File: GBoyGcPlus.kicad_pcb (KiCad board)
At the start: 2 copper layers, 62.9 x 53.1 mm, 43 parts, among them J1 Conn_01x06, J2 Conn_01x06, J3 Left Stick, J4 Right Stick, SW1 RKA2SGG055SMTR LFS, SW2 RKA2SGG055SMTR LFS, SW3 RKA2SGG055SMTR LFS, SW4 RKA2SGG055SMTR LFS, SW5 RKA2SGG055SMTR LFS, SW6 RKA2SGG055SMTR LFS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

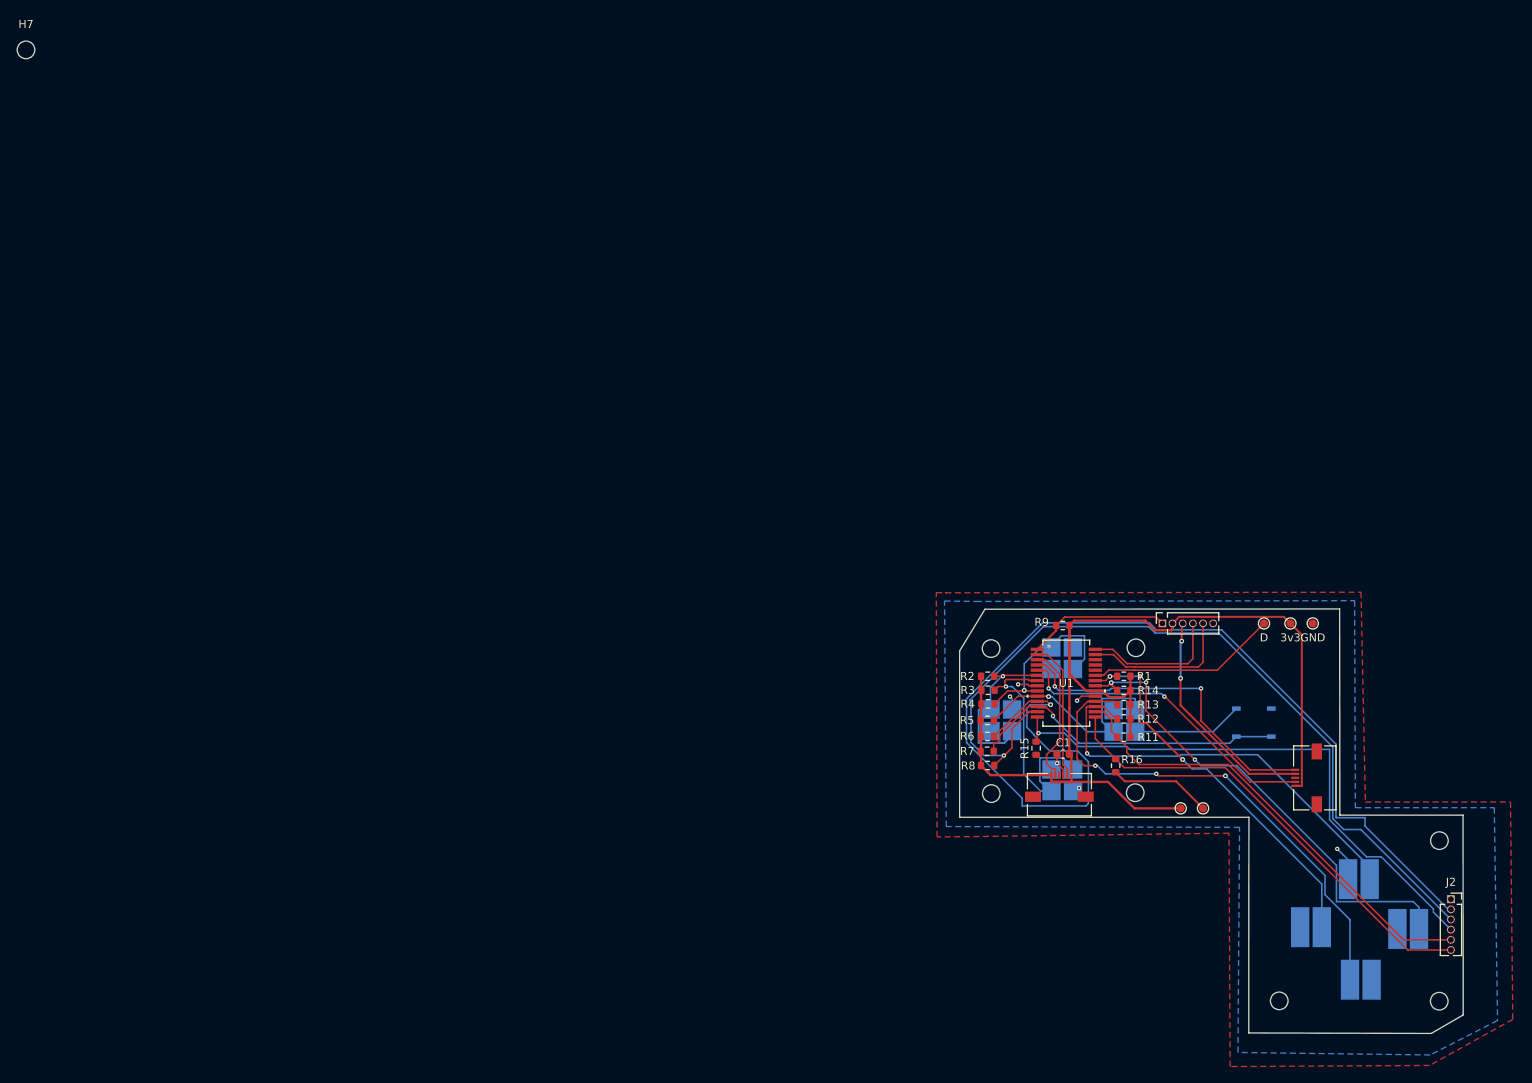
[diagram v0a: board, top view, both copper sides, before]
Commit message: Changed PCB to use GC2 Micro controller
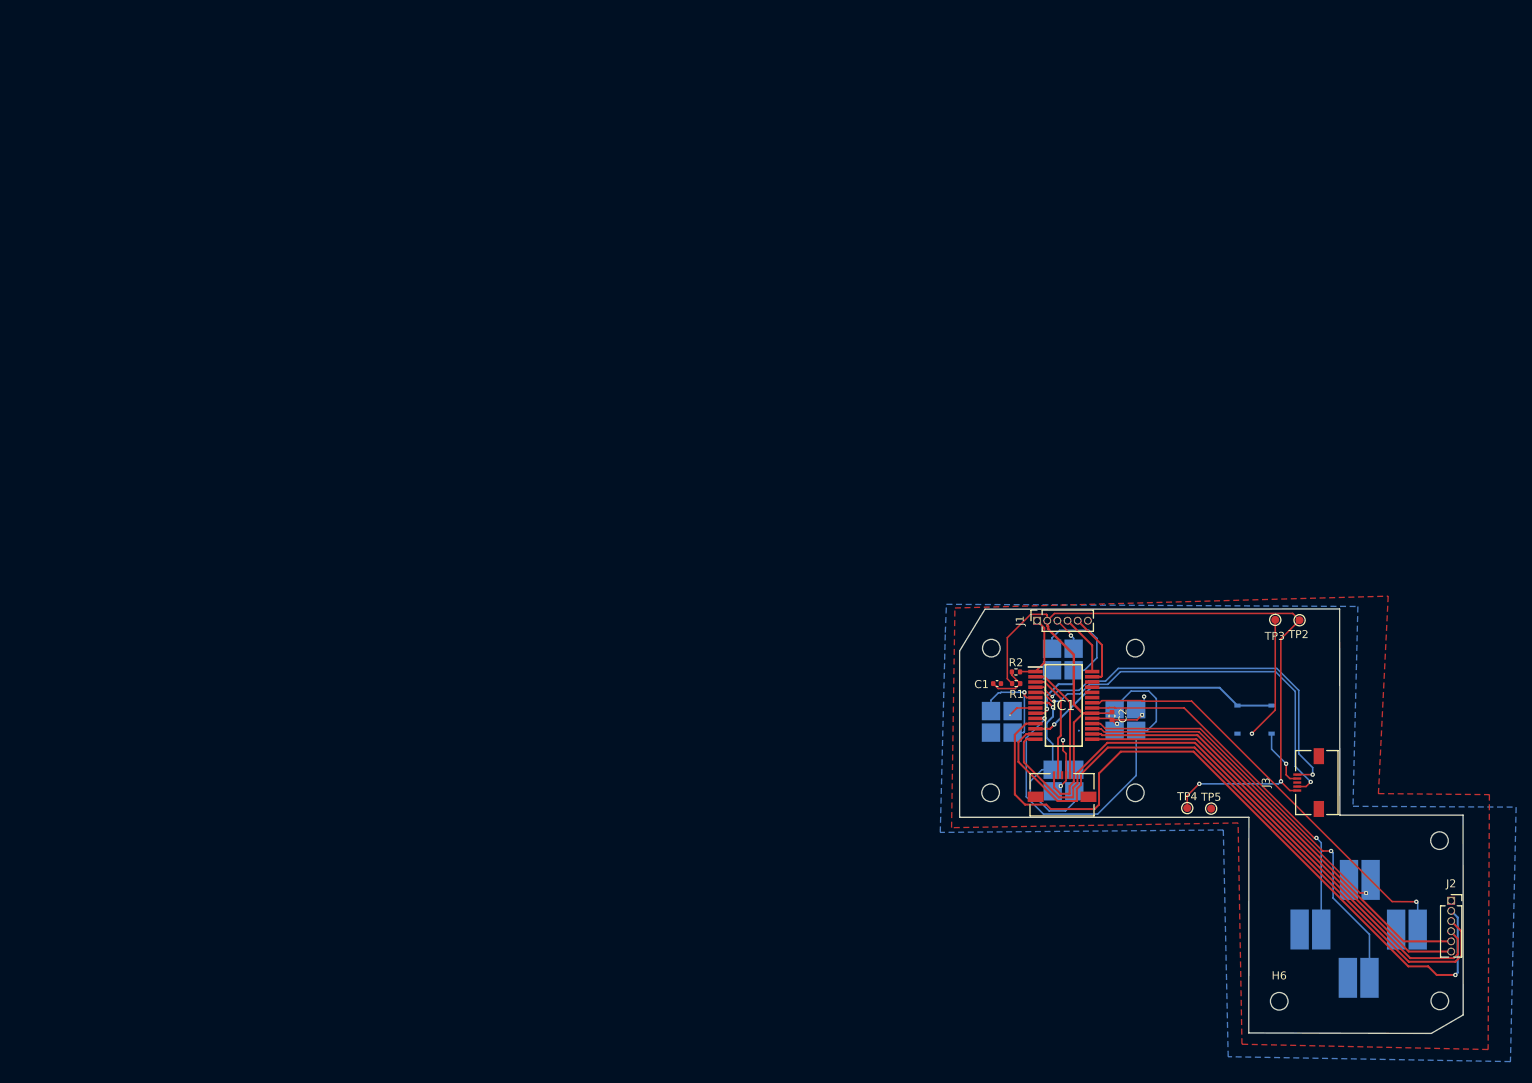
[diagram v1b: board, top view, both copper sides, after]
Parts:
- removed 3v3: 3v3, TestPoint:TestPoint_Pad_D1.0mm
- removed D: D, TestPoint:TestPoint_Pad_D1.0mm
- removed GND: Gnd, TestPoint:TestPoint_Pad_D1.0mm
- removed H4: MountingHole, MountingHole:MountingHole_2.2mm_M2
- removed R11, R12, R13, R14, R15, R16, R3, R4, R5, R6, R7, R8, R9: 10k, Resistor_SMD:R_0603_1608Metric
- removed U1: pic18f25k22-i/ss, GCPlus:SSOP28_MC_MCH
- added C2: 0.1uf, Capacitor_SMD:C_0402_1005Metric, F.Cu at (138.2, 85.7)
- added IC1: PIC18F25K42-I_SS, GCPlus:SOP65P780X200-28N, F.Cu at (132.2, 84.4)
- added TP2: 3v3, TestPoint:TestPoint_Pad_D1.0mm, F.Cu at (161.7, 73.8)
- added TP3: Gnd, TestPoint:TestPoint_Pad_D1.0mm, F.Cu at (158.6, 73.7)
- C1: value 100 nF -> 0.1uF; footprint Capacitor_SMD:C_0603_1608Metric -> Capacitor_SMD:C_0402_1005Metric
- R1: footprint Resistor_SMD:R_0603_1608Metric -> Resistor_SMD:R_0402_1005Metric
- R2: value 10k -> 1000Ohm; footprint Resistor_SMD:R_0603_1608Metric -> Resistor_SMD:R_0402_1005Metric
- SW5, SW6, SW7, SW8: footprint footprints:DPAD -> GCPlus:DPAD
- SW9: footprint footprints:RKA2SG_CNK -> GCPlus:RKA2SG_CNK-L
- moved H7 202.5 mm to (179.2, 101.3)
- moved H3 25.6 mm to (141.1, 77.3)
- moved H1 25.5 mm to (141.1, 95.3)
- moved H5 18.1 mm to (123.1, 77.3)
- moved H2 18.1 mm to (123.0, 95.3)
- moved J1 15.7 mm to (128.9, 73.8)
- moved R1 13.5 mm to (126.2, 81.7)
- moved SW6 12.2 mm to (164.4, 112.4)
- moved C1 12.1 mm to (123.9, 81.7)
- moved SW5 12.0 mm to (176.4, 112.4)
- moved R2 3.58 mm to (126.2, 80.2)
- moved SW3 2.79 mm to (133.4, 77.3), turned to 180 degrees
- moved SW1 2.51 mm to (125.8, 85.1), turned to 180 degrees
- moved SW7 2.44 mm to (170.4, 118.5), turned to 180 degrees
- moved TP5 1.01 mm to (150.6, 97.3)
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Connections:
- C1 pad 1: GND -> Net-(C1-Pad1)
- C1 pad 2: +3V3 -> GND
- R1 pad 1: /DL -> +3V3
- R1 pad 2: +3V3 -> Net-(C1-Pad1)
- R2 pad 1: +3V3 -> Net-(C1-Pad1)
- R2 pad 2: /A -> /MCLR
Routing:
- net /Z: track 139.3 -> 91.7 mm
- net Net-(U1-RB2): track 23.8 -> 0.00 mm
- net /RT: track 104.9 -> 83.1 mm, vias 1 -> 0
- net GND: track 70.1 -> 49.4 mm, vias 8 -> 9
- net +3V3: track 134.6 -> 115.6 mm, vias 0 -> 2
- net /Y: track 28.5 -> 46.6 mm
- net /DR: track 61.1 -> 46.5 mm, vias 3 -> 1
- net /SY: track 39.1 -> 49.8 mm
- net /DU: track 53.2 -> 42.7 mm
- net /PGD: track 17.6 -> 7.64 mm
- net /PGC: track 19.2 -> 9.43 mm
- net /B: track 33.0 -> 23.9 mm
- net /S: track 41.6 -> 32.6 mm
- net /MCLR: track 18.0 -> 9.13 mm
- net /R: track 70.4 -> 79.2 mm, vias 1 -> 0
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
